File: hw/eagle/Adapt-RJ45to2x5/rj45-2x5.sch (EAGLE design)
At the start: 5 parts, among them P11 SOLPAD035, P21 SOLPAD035

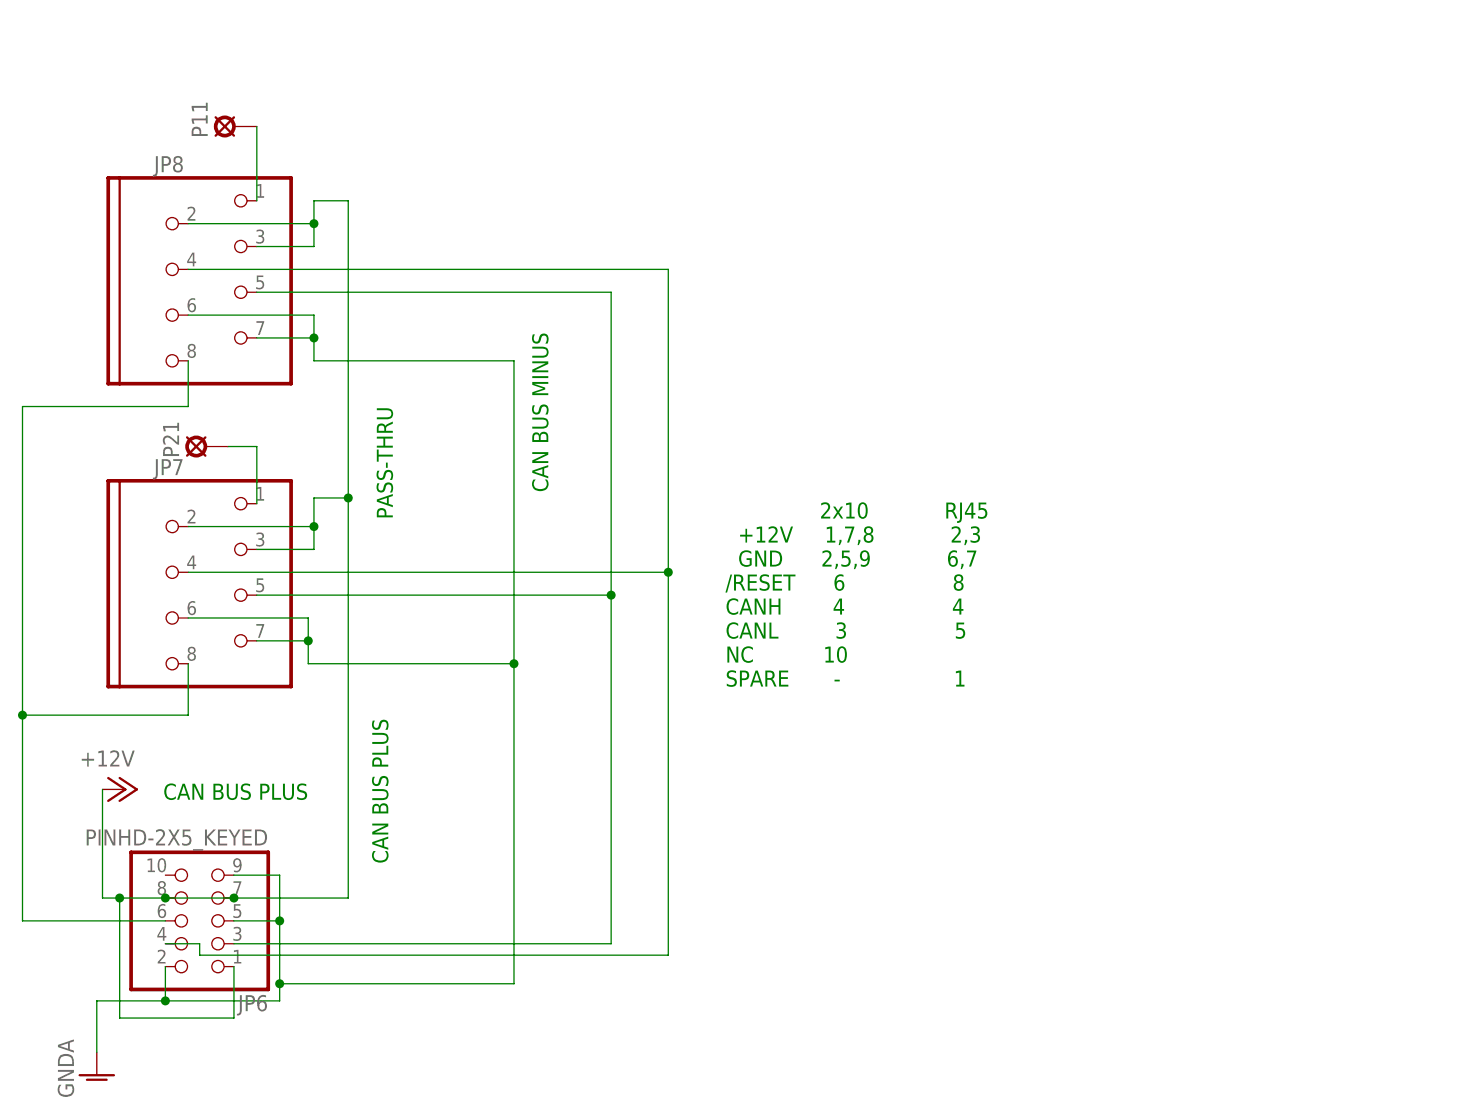
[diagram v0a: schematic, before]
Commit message: add rj45-2x10 adaptor eagle files
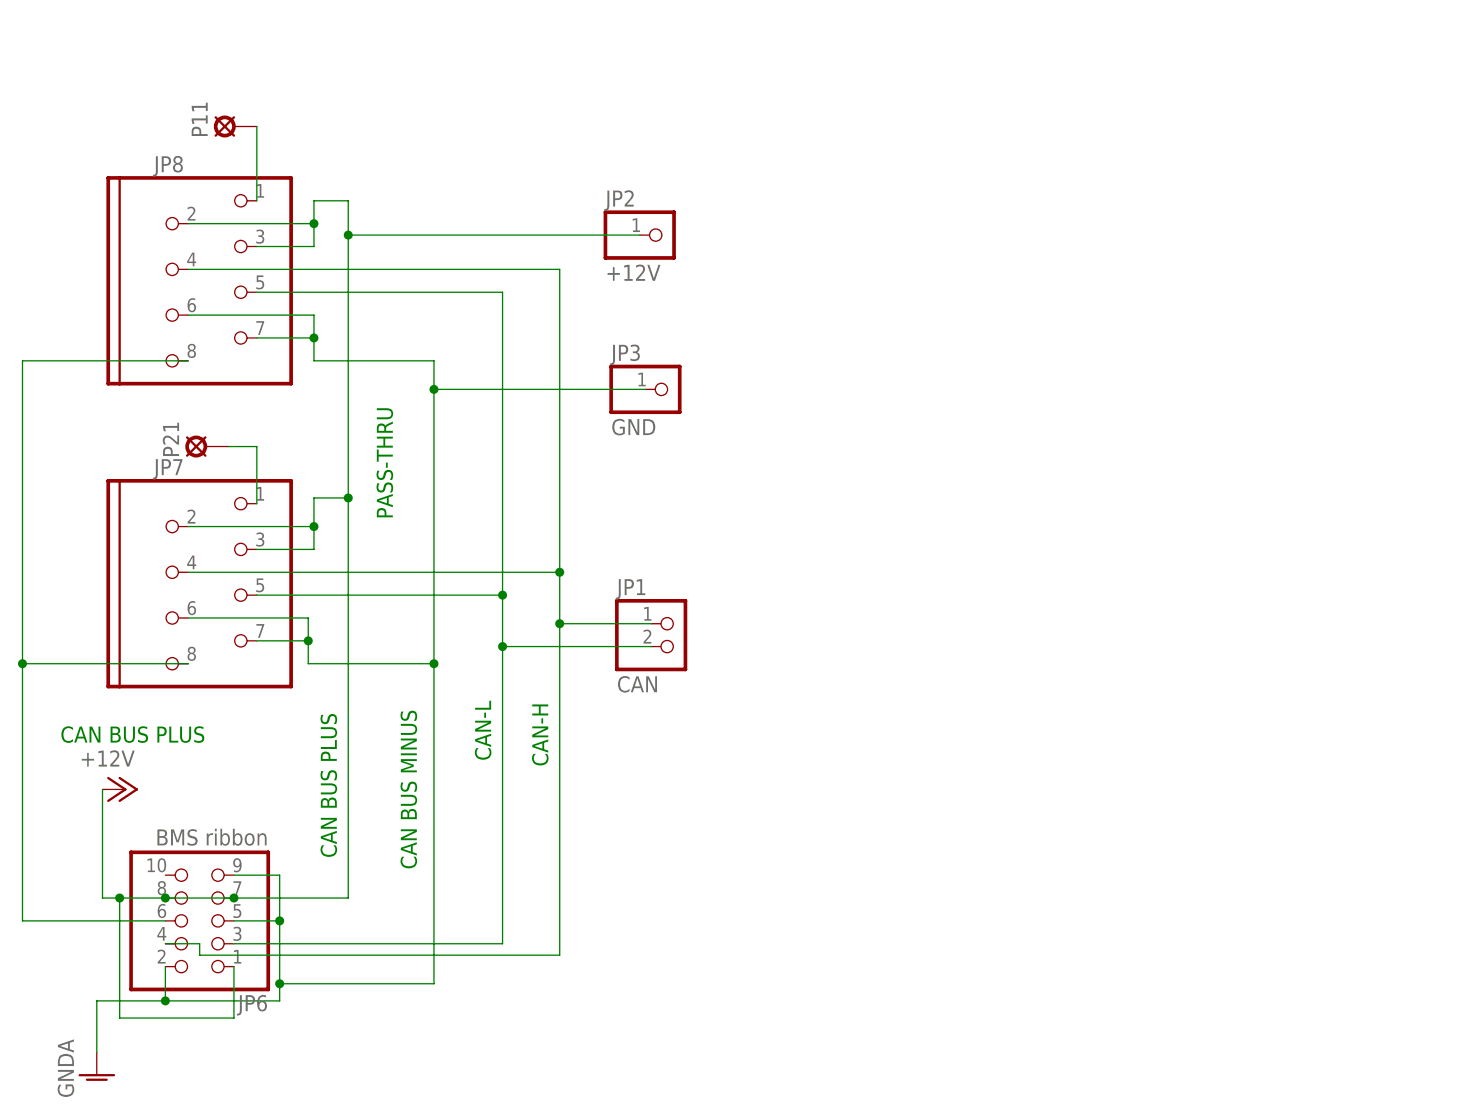
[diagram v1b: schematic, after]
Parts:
- added JP1: CAN, pinhead:PINHD-1X2
- added JP2: +12V, pinhead:PINHD-1X1
- added JP3: GND, pinhead:PINHD-1X1
- JP6: value PINHD-2X5_KEYED -> BMS ribbon
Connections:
- net +12V: now also JP2.1
- net CANH: now also JP1.1
- net CANL: now also JP1.2
- net GNDA: now also JP3.1
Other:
- note added: "CAN-H"
- note added: "CAN-L"
- note removed: "2x10 RJ45 +12V 1,7,8 2,3 GND 2,5,9 6,7 /RESET 6 8 CANH 4 4 CANL 3 5 NC 10 SPARE - 1"
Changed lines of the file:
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@@
 <parts>
 <part name="P+1" library="supply1" deviceset="+12V" device=""/>
-<part name="JP6" library="pinhead" deviceset="PINHD-2X5_KEYED" device=""/>
+<part name="JP6" library="pinhead" deviceset="PINHD-2X5_KEYED" device="" value="BMS ribbon"/>
 <part name="GND10" library="supply1" deviceset="GNDA" device=""/>
 <part name="JP7" library="DEH" deviceset="MOD8P8C" device=""/>
@@
 <part name="P11" library="solpad" deviceset="SOLPAD035" device=""/>
 <part name="P21" library="solpad" deviceset="SOLPAD035" device=""/>
+<part name="JP1" library="pinhead" deviceset="PINHD-1X2" device="" value="CAN"/>
+<part name="JP2" library="pinhead" deviceset="PINHD-1X1" device="" value="+12V"/>
+<part name="JP3" library="pinhead" deviceset="PINHD-1X1" device="" value="GND"/>
 </parts>
 <sheets>
 <sheet>
 <plain>
-<text x="40.005" y="47.625" size="1.778" layer="91" rot="R180">CAN BUS PLUS</text>
+<text x="28.575" y="53.975" size="1.778" layer="91" rot="R180">CAN BUS PLUS</text>
 <text x="47.625" y="89.535" size="1.778" layer="91" rot="R270">PASS-THRU</text>
-<text x="48.895" y="38.735" size="1.778" layer="91" rot="R90">CAN BUS PLUS</text>
-<text x="66.675" y="80.01" size="1.778" layer="91" rot="R90">CAN BUS MINUS</text>
-<text x="86.36" y="58.42" size="1.778" layer="91">               2x10            RJ45
-  +12V     1,7,8            2,3
-  GND      2,5,9            6,7
-/RESET      6                 8
-CANH        4                 4
-CANL         3                 5
-NC           10
-SPARE       -                  1</text>
+<text x="43.18" y="39.37" size="1.778" layer="91" rot="R90">CAN BUS PLUS</text>
+<text x="52.07" y="38.1" size="1.778" layer="91" rot="R90">CAN BUS MINUS</text>
+<text x="66.675" y="49.53" size="1.778" layer="91" rot="R90">CAN-H</text>
+<text x="60.325" y="50.165" size="1.778" layer="91" rot="R90">CAN-L</text>
 </plain>
 <instances>
@@
 <instance part="P11" gate="G$1" x="31.75" y="120.65" rot="R90"/>
 <instance part="P21" gate="G$1" x="28.575" y="85.09" rot="R90"/>
+<instance part="JP1" gate="G$1" x="80.645" y="62.865"/>
+<instance part="JP2" gate="G$1" x="79.375" y="108.585"/>
+<instance part="JP3" gate="G$1" x="80.01" y="91.44"/>
 </instances>
 <busses>
@@
 <net name="GNDA" class="0">
 <segment>
-<wire x1="62.865" y1="60.96" x2="62.865" y2="94.615" width="0.1524" layer="91"/>
-<wire x1="40.005" y1="60.96" x2="62.865" y2="60.96" width="0.1524" layer="91"/>
+<wire x1="53.975" y1="60.96" x2="53.975" y2="91.44" width="0.1524" layer="91"/>
+<wire x1="53.975" y1="91.44" x2="53.975" y2="94.615" width="0.1524" layer="91"/>
+<wire x1="40.005" y1="60.96" x2="53.975" y2="60.96" width="0.1524" layer="91"/>
 <wire x1="34.29" y1="63.5" x2="40.005" y2="63.5" width="0.1524" layer="91"/>
 <wire x1="26.67" y1="66.04" x2="40.005" y2="66.04" width="0.1524" layer="91"/>
 <wire x1="40.005" y1="66.04" x2="40.005" y2="63.5" width="0.1524" layer="91"/>
 <wire x1="40.005" y1="63.5" x2="40.005" y2="60.96" width="0.1524" layer="91"/>
-<wire x1="40.64" y1="94.615" x2="62.865" y2="94.615" width="0.1524" layer="91"/>
+<wire x1="40.64" y1="94.615" x2="53.975" y2="94.615" width="0.1524" layer="91"/>
 <wire x1="34.29" y1="97.155" x2="40.64" y2="97.155" width="0.1524" layer="91"/>
 <wire x1="40.64" y1="97.155" x2="40.64" y2="94.615" width="0.1524" layer="91"/>
@@
 <wire x1="36.83" y1="32.385" x2="31.75" y2="32.385" width="0.1524" layer="91"/>
 <wire x1="36.83" y1="32.385" x2="36.83" y2="25.4" width="0.1524" layer="91"/>
-<wire x1="36.83" y1="25.4" x2="62.865" y2="25.4" width="0.1524" layer="91"/>
+<wire x1="36.83" y1="25.4" x2="53.975" y2="25.4" width="0.1524" layer="91"/>
 <wire x1="36.83" y1="25.4" x2="36.83" y2="23.495" width="0.1524" layer="91"/>
 <wire x1="36.83" y1="23.495" x2="24.13" y2="23.495" width="0.1524" layer="91"/>
@@
 <pinref part="JP6" gate="G$1" pin="9"/>
 <pinref part="GND10" gate="1" pin="GNDA"/>
-<wire x1="62.865" y1="60.96" x2="62.865" y2="25.4" width="0.1524" layer="91"/>
-<junction x="62.865" y="60.96"/>
+<wire x1="53.975" y1="60.96" x2="53.975" y2="25.4" width="0.1524" layer="91"/>
+<junction x="53.975" y="60.96"/>
+<pinref part="JP3" gate="G$1" pin="1"/>
+<wire x1="77.47" y1="91.44" x2="53.975" y2="91.44" width="0.1524" layer="91"/>
+<junction x="53.975" y="91.44"/>
 </segment>
 </net>
@@
 <wire x1="40.64" y1="109.855" x2="40.64" y2="112.395" width="0.1524" layer="91"/>
 <wire x1="40.64" y1="112.395" x2="44.45" y2="112.395" width="0.1524" layer="91"/>
-<wire x1="44.45" y1="79.375" x2="44.45" y2="112.395" width="0.1524" layer="91"/>
+<wire x1="44.45" y1="79.375" x2="44.45" y2="108.585" width="0.1524" layer="91"/>
+<wire x1="44.45" y1="108.585" x2="44.45" y2="112.395" width="0.1524" layer="91"/>
 <wire x1="44.45" y1="79.375" x2="40.64" y2="79.375" width="0.1524" layer="91"/>
 <wire x1="34.29" y1="73.66" x2="40.64" y2="73.66" width="0.1524" layer="91"/>
@@
 <wire x1="44.45" y1="79.375" x2="44.45" y2="34.925" width="0.1524" layer="91"/>
 <junction x="44.45" y="79.375"/>
+<pinref part="JP2" gate="G$1" pin="1"/>
+<wire x1="76.835" y1="108.585" x2="44.45" y2="108.585" width="0.1524" layer="91"/>
+<junction x="44.45" y="108.585"/>
 </segment>
 </net>
 <net name="CANL" class="0">
 <segment>
-<wire x1="34.29" y1="68.58" x2="73.66" y2="68.58" width="0.1524" layer="91"/>
+<wire x1="34.29" y1="68.58" x2="61.595" y2="68.58" width="0.1524" layer="91"/>
 <pinref part="JP7" gate="G$1" pin="3"/>
-<wire x1="73.66" y1="68.58" x2="73.66" y2="29.845" width="0.1524" layer="91"/>
-<wire x1="31.75" y1="29.845" x2="73.66" y2="29.845" width="0.1524" layer="91"/>
+<wire x1="61.595" y1="68.58" x2="61.595" y2="62.865" width="0.1524" layer="91"/>
+<wire x1="61.595" y1="62.865" x2="61.595" y2="29.845" width="0.1524" layer="91"/>
+<wire x1="31.75" y1="29.845" x2="61.595" y2="29.845" width="0.1524" layer="91"/>
 <pinref part="JP6" gate="G$1" pin="3"/>
 <pinref part="JP8" gate="G$1" pin="3"/>
-<wire x1="34.29" y1="102.235" x2="73.66" y2="102.235" width="0.1524" layer="91"/>
-<wire x1="73.66" y1="68.58" x2="73.66" y2="102.235" width="0.1524" layer="91"/>
-<junction x="73.66" y="68.58"/>
+<wire x1="34.29" y1="102.235" x2="61.595" y2="102.235" width="0.1524" layer="91"/>
+<wire x1="61.595" y1="68.58" x2="61.595" y2="102.235" width="0.1524" layer="91"/>
+<junction x="61.595" y="68.58"/>
+<pinref part="JP1" gate="G$1" pin="2"/>
+<wire x1="78.105" y1="62.865" x2="61.595" y2="62.865" width="0.1524" layer="91"/>
+<junction x="61.595" y="62.865"/>
 </segment>
 </net>
 <net name="CANH" class="0">
 <segment>
-<wire x1="26.67" y1="71.12" x2="80.01" y2="71.12" width="0.1524" layer="91"/>
+<wire x1="26.67" y1="71.12" x2="67.945" y2="71.12" width="0.1524" layer="91"/>
 <pinref part="JP7" gate="G$1" pin="6"/>
 <wire x1="27.94" y1="29.845" x2="27.94" y2="28.575" width="0.1524" layer="91"/>
-<wire x1="27.94" y1="28.575" x2="80.01" y2="28.575" width="0.1524" layer="91"/>
-<wire x1="80.01" y1="71.12" x2="80.01" y2="28.575" width="0.1524" layer="91"/>
+<wire x1="27.94" y1="28.575" x2="67.945" y2="28.575" width="0.1524" layer="91"/>
+<wire x1="67.945" y1="71.12" x2="67.945" y2="65.405" width="0.1524" layer="91"/>
 <pinref part="JP6" gate="G$1" pin="4"/>
+<wire x1="67.945" y1="65.405" x2="67.945" y2="28.575" width="0.1524" layer="91"/>
 <wire x1="27.94" y1="29.845" x2="24.13" y2="29.845" width="0.1524" layer="91"/>
 <pinref part="JP8" gate="G$1" pin="6"/>
-<wire x1="26.67" y1="104.775" x2="80.01" y2="104.775" width="0.1524" layer="91"/>
-<wire x1="80.01" y1="71.12" x2="80.01" y2="104.775" width="0.1524" layer="91"/>
-<junction x="80.01" y="71.12"/>
+<wire x1="26.67" y1="104.775" x2="67.945" y2="104.775" width="0.1524" layer="91"/>
+<wire x1="67.945" y1="71.12" x2="67.945" y2="104.775" width="0.1524" layer="91"/>
+<junction x="67.945" y="71.12"/>
+<pinref part="JP1" gate="G$1" pin="1"/>
+<wire x1="78.105" y1="65.405" x2="67.945" y2="65.405" width="0.1524" layer="91"/>
+<junction x="67.945" y="65.405"/>
 </segment>
 </net>
@@
 <net name="MASTER-RESET-SYS" class="0">
 <segment>
-<wire x1="26.67" y1="55.245" x2="26.67" y2="60.96" width="0.1524" layer="91"/>
 <pinref part="JP7" gate="G$1" pin="8"/>
 <wire x1="24.13" y1="32.385" x2="8.255" y2="32.385" width="0.1524" layer="91"/>
 <pinref part="JP6" gate="G$1" pin="6"/>
-<wire x1="26.67" y1="55.245" x2="8.255" y2="55.245" width="0.1524" layer="91"/>
-<wire x1="8.255" y1="55.245" x2="8.255" y2="32.385" width="0.1524" layer="91"/>
-<wire x1="8.255" y1="55.245" x2="8.255" y2="89.535" width="0.1524" layer="91"/>
-<junction x="8.255" y="55.245"/>
+<wire x1="26.67" y1="60.96" x2="8.255" y2="60.96" width="0.1524" layer="91"/>
+<wire x1="8.255" y1="60.96" x2="8.255" y2="32.385" width="0.1524" layer="91"/>
+<wire x1="8.255" y1="60.96" x2="8.255" y2="94.615" width="0.1524" layer="91"/>
+<junction x="8.255" y="60.96"/>
 <pinref part="JP8" gate="G$1" pin="8"/>
-<wire x1="8.255" y1="89.535" x2="26.67" y2="89.535" width="0.1524" layer="91"/>
-<wire x1="26.67" y1="89.535" x2="26.67" y2="94.615" width="0.1524" layer="91"/>
+<wire x1="8.255" y1="94.615" x2="26.67" y2="94.615" width="0.1524" layer="91"/>
 </segment>
 </net>
@@
 </schematic>
 </drawing>
-<compatibility>
-<note version="6.3" minversion="6.2.2" severity="warning">
-Since Version 6.2.2 text objects can contain more than one line,
-which will not be processed correctly with this version.
-</note>
-</compatibility>
 </eagle>

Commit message: save work and backup
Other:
- note added: "Adaptor"
- note added: "BMS pcb 2x10 keyed header"
- note added: "RJ45 CAN cable"
- note added: "to"
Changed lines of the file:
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@@
 <text x="66.675" y="49.53" size="1.778" layer="91" rot="R90">CAN-H</text>
 <text x="60.325" y="50.165" size="1.778" layer="91" rot="R90">CAN-L</text>
+<text x="48.26" y="127" size="3.81" layer="91">Adaptor</text>
+<text x="76.2" y="127" size="3.81" layer="91">RJ45 CAN cable</text>
+<text x="96.52" y="121.92" size="3.81" layer="91">to</text>
+<text x="83.82" y="116.84" size="3.81" layer="91">BMS pcb 2x10 keyed header</text>
 </plain>
 <instances>
